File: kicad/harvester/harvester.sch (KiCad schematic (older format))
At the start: 33 parts, among them P1 CONN_5, P2 CONN_12X2, SW1 SW_PUSH_SMALL, U1 PANSTAMP_02, U2 BMP085, U3 DHT22, U4 BQ25504, U5 TMP36

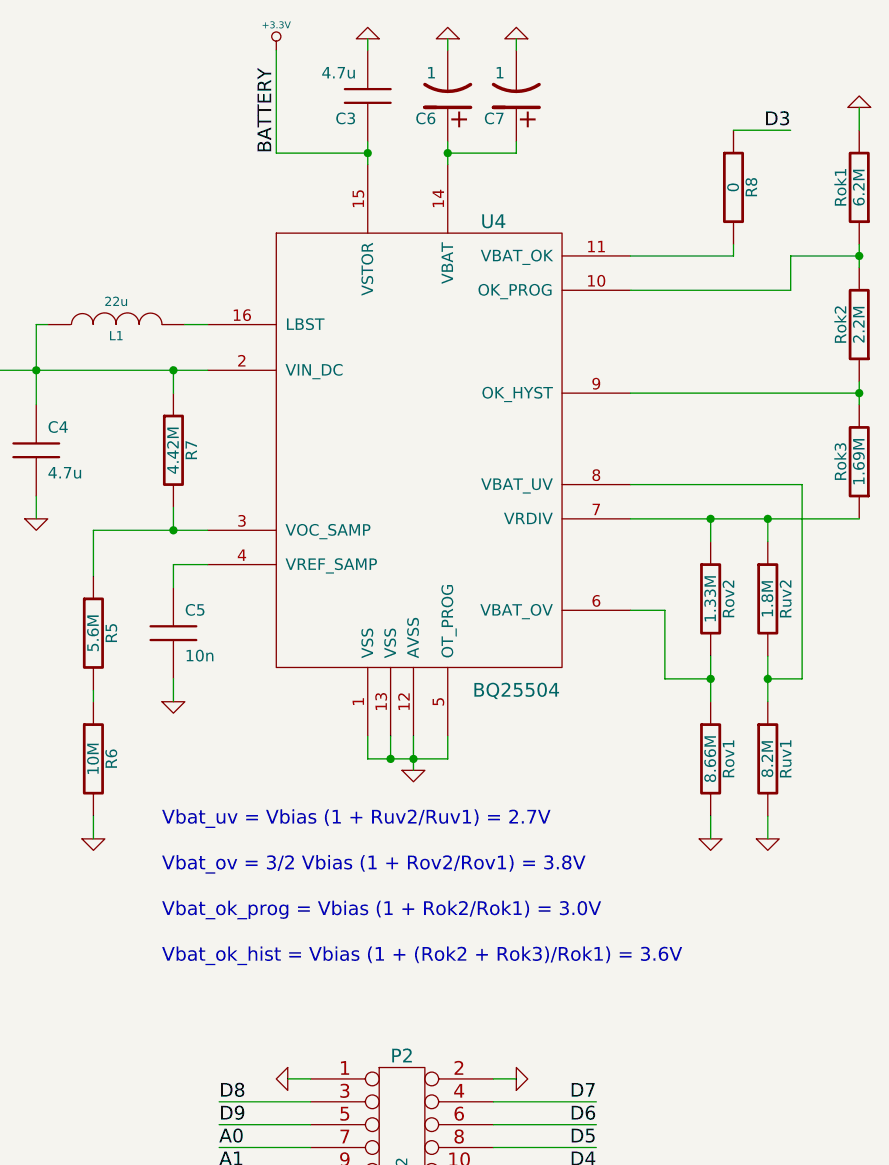
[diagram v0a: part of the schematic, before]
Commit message: Updated resistor values
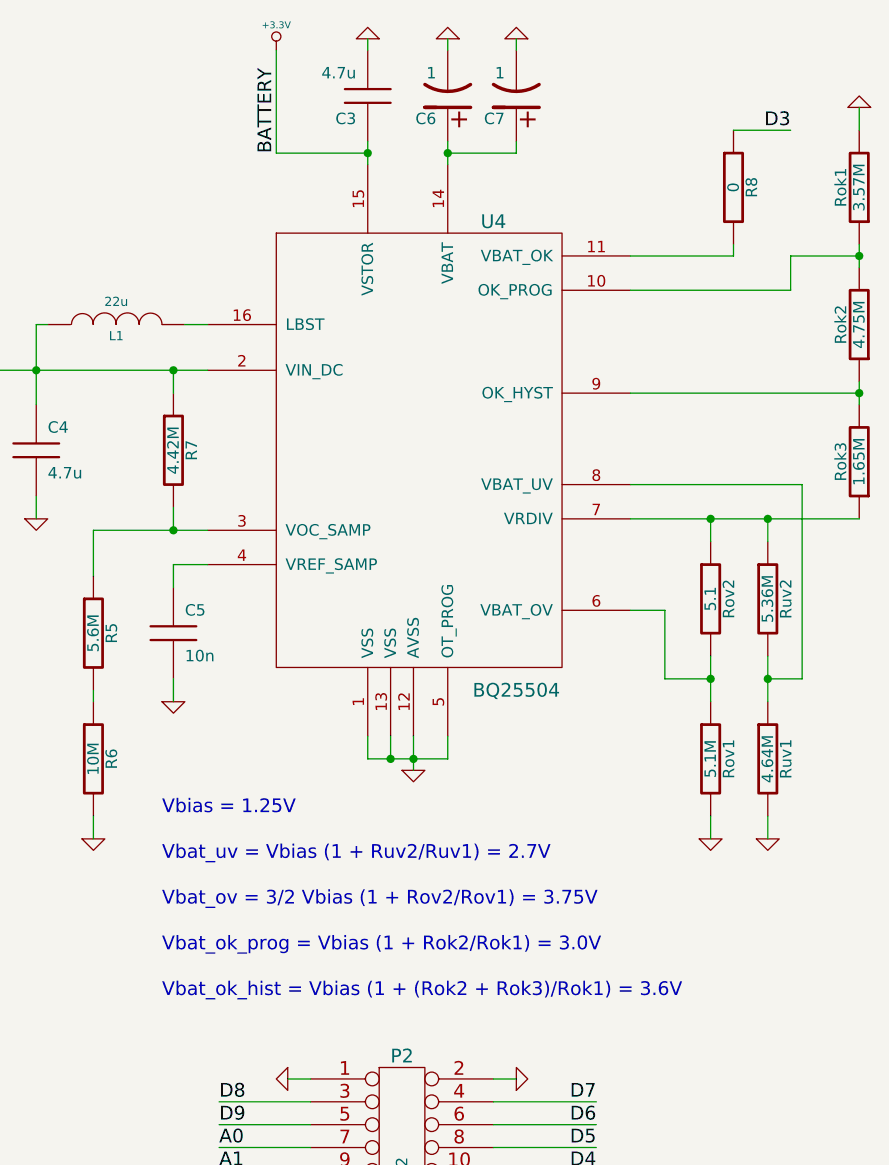
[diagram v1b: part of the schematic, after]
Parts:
- Rok1: value 6.2M -> 3.57M
- Rok2: value 2.2M -> 4.75M
- Rok3: value 1.69M -> 1.65M
- Rov1: value 8.66M -> 5.1M
- Rov2: value 1.33M -> 5.1
- Ruv1: value 8.2M -> 4.64M
- Ruv2: value 1.8M -> 5.36M
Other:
- note added: "Vbat_ov = 3/2 Vbias (1 + Rov2/Rov1) = 3.75V"
- note added: "Vbias = 1.25V"
- note removed: "Vbat_ov = 3/2 Vbias (1 + Rov2/Rov1) = 3.8V"
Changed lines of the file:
@@
-EESchema Schematic File Version 2  date Mon 11 Jun 2012 06:13:37 PM CEST
+EESchema Schematic File Version 2  date Wed 26 Sep 2012 01:37:27 PM CEST
 LIBS:power
 LIBS:device
@@
 Sheet 1 1
 Title "panStamp solar harvester"
-Date "11 jun 2012"
+Date "26 sep 2012"
 Rev "01"
 Comp "uSAPIENS"
@@
 Comment4 ""
 $EndDescr
+Text Notes 7450 4350 0    60   ~ 0
+Vbias = 1.25V
 Wire Wire Line
 	8700 1450 9000 1450
@@
 Text Notes 5750 2250 0    60   ~ 0
 open circuit = 2.2V
-Text Notes 7450 4800 0    60   ~ 0
+Text Notes 7450 4950 0    60   ~ 0
 Vbat_ok_prog = Vbias (1 + Rok2/Rok1) = 3.0V
-Text Notes 7450 5000 0    60   ~ 0
+Text Notes 7450 5150 0    60   ~ 0
 Vbat_ok_hist = Vbias (1 + (Rok2 + Rok3)/Rok1) = 3.6V
-Text Notes 7450 4600 0    60   ~ 0
-Vbat_ov = 3/2 Vbias (1 + Rov2/Rov1) = 3.8V
-Text Notes 7450 4400 0    60   ~ 0
+Text Notes 7450 4750 0    60   ~ 0
+Vbat_ov = 3/2 Vbias (1 + Rov2/Rov1) = 3.75V
+Text Notes 7450 4550 0    60   ~ 0
 Vbat_uv = Vbias (1 + Ruv2/Ruv1) = 2.7V
 $Comp
@@
 P 10500 1600
 F 0 "Rok1" V 10580 1600 50  0000 C CNN
-F 1 "6.2M" V 10500 1600 50  0000 C CNN
+F 1 "3.57M" V 10500 1600 50  0000 C CNN
 F 2 "SM0603S" H 10500 1600 60  0001 C CNN
 	1    10500 1600
@@
 P 10500 2800
 F 0 "Rok3" V 10580 2800 50  0000 C CNN
-F 1 "1.69M" V 10500 2800 50  0000 C CNN
+F 1 "1.65M" V 10500 2800 50  0000 C CNN
 F 2 "SM0603S" H 10500 2800 60  0001 C CNN
 	1    10500 2800
@@
 P 10500 2200
 F 0 "Rok2" V 10580 2200 50  0000 C CNN
-F 1 "2.2M" V 10500 2200 50  0000 C CNN
+F 1 "4.75M" V 10500 2200 50  0000 C CNN
 F 2 "SM0603S" H 10500 2200 60  0001 C CNN
 	1    10500 2200
@@
 P 10100 3400
 F 0 "Ruv2" V 10180 3400 50  0000 C CNN
-F 1 "1.8M" V 10100 3400 50  0000 C CNN
+F 1 "5.36M" V 10100 3400 50  0000 C CNN
 F 2 "SM0603S" H 10100 3400 60  0001 C CNN
 	1    10100 3400
@@
 P 10100 4100
 F 0 "Ruv1" V 10180 4100 50  0000 C CNN
-F 1 "8.2M" V 10100 4100 50  0000 C CNN
+F 1 "4.64M" V 10100 4100 50  0000 C CNN
 F 2 "SM0603S" H 10100 4100 60  0001 C CNN
 	1    10100 4100
@@
 P 9850 4100
 F 0 "Rov1" V 9930 4100 50  0000 C CNN
-F 1 "8.66M" V 9850 4100 50  0000 C CNN
+F 1 "5.1M" V 9850 4100 50  0000 C CNN
 F 2 "SM0603S" H 9850 4100 60  0001 C CNN
 	1    9850 4100
@@
 P 9850 3400
 F 0 "Rov2" V 9930 3400 50  0000 C CNN
-F 1 "1.33M" V 9850 3400 50  0000 C CNN
+F 1 "5.1" V 9850 3400 50  0000 C CNN
 F 2 "SM0603S" H 9850 3400 60  0001 C CNN
 	1    9850 3400
